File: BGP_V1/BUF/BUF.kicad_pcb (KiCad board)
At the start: 2 copper layers, 30 x 30 mm, 23 parts, among them P1 CONN_01X05, P2 CONN_01X02, P3 CONN_01X12, U1 MC33178, U2 TLV170

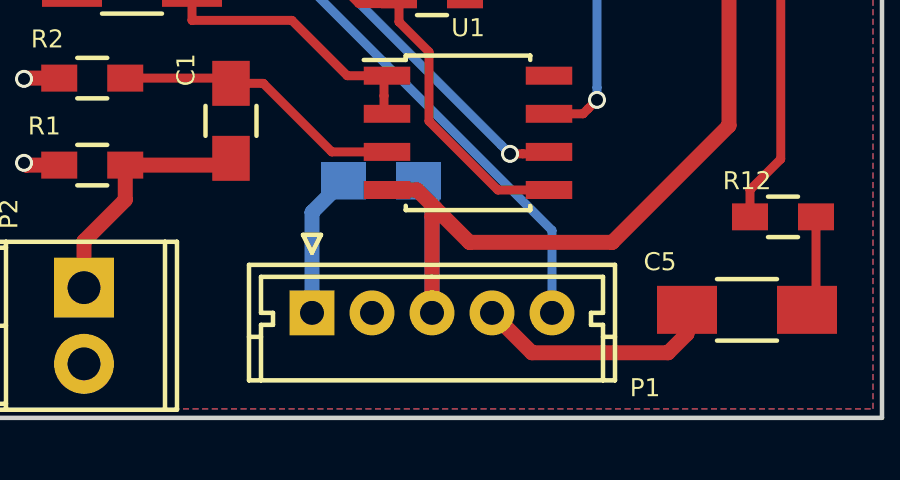
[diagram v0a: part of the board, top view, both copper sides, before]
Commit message: Gerbers
Mainly getting gerbers ready.  Issue with pots overlapping other boards in silk screens - top and bottom.
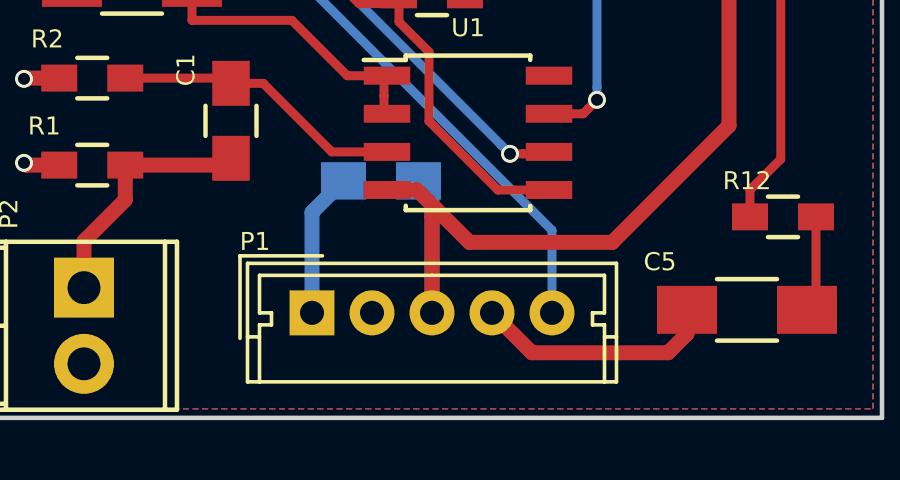
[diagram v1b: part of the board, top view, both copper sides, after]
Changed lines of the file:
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@@
-(kicad_pcb (version 4) (host pcbnew 4.0.4-1.fc24-product)
+(kicad_pcb (version 4) (host pcbnew 4.0.7)
   (general
     (links 49)
     (no_connects 0)
-    (area 135.10412 74.424999 167.075001 122.285001)
+    (area 135.10412 74.424999 167.075001 122.779999)
     (thickness 1.6)
     (drawings 9)
@@
       (drillshape 0)
       (scaleselection 1)
-      (outputdirectory ../../BGP/GERBER/BUF_1/))
+      (outputdirectory ../../GERBER/BUF_1/))
   )
   (net 0 "")
@@
     )
   )
-  (module Connectors_Molex:Molex_MicroLatch-53253-0570_05x2.00mm_Straight (layer F.Cu)
-    (at 148 118.5)
-    (descr "Molex Micro-Latch connector, PN:53253-0570, top entry type, through hole")
-    (tags "conn molex micro latch")
-    (fp_text reference P1 (at 11.1 2.5) (layer F.SilkS)
-      (effects (font (size 0.6 0.6) (thickness 0.15)))
-    )
-    (fp_text value CONN_01X05 (at 4 -3.5) (layer F.Fab) hide
-      (effects (font (size 0.6 0.6) (thickness 0.15)))
-    )
-    (fp_line (start -2.6 -2.1) (end -2.6 2.75) (layer F.CrtYd) (width 0.05))
-    (fp_line (start -2.6 2.75) (end 10.55 2.75) (layer F.CrtYd) (width 0.05))
-    (fp_line (start 10.55 2.75) (end 10.55 -2.1) (layer F.CrtYd) (width 0.05))
-    (fp_line (start 10.55 -2.1) (end -2.6 -2.1) (layer F.CrtYd) (width 0.05))
-    (fp_line (start -2.1 -1.6) (end -2.1 2.25) (layer F.SilkS) (width 0.15))
-    (fp_line (start -2.1 2.25) (end 10.1 2.25) (layer F.SilkS) (width 0.15))
-    (fp_line (start 10.1 2.25) (end 10.1 -1.6) (layer F.SilkS) (width 0.15))
-    (fp_line (start 10.1 -1.6) (end -2.1 -1.6) (layer F.SilkS) (width 0.15))
-    (fp_line (start 0 -2) (end -0.3 -2.6) (layer F.SilkS) (width 0.15))
-    (fp_line (start -0.3 -2.6) (end 0.3 -2.6) (layer F.SilkS) (width 0.15))
-    (fp_line (start 0.3 -2.6) (end 0 -2) (layer F.SilkS) (width 0.15))
-    (fp_line (start -2.1 0.8) (end -1.7 0.8) (layer F.SilkS) (width 0.15))
-    (fp_line (start 10.1 0.8) (end 9.7 0.8) (layer F.SilkS) (width 0.15))
-    (fp_line (start 4 -1.2) (end -1.7 -1.2) (layer F.SilkS) (width 0.15))
-    (fp_line (start -1.7 -1.2) (end -1.7 0) (layer F.SilkS) (width 0.15))
-    (fp_line (start -1.7 0) (end -1.3 0) (layer F.SilkS) (width 0.15))
-    (fp_line (start -1.3 0) (end -1.3 0.4) (layer F.SilkS) (width 0.15))
-    (fp_line (start -1.3 0.4) (end -1.7 0.4) (layer F.SilkS) (width 0.15))
-    (fp_line (start -1.7 0.4) (end -1.7 2.25) (layer F.SilkS) (width 0.15))
-    (fp_line (start 4 -1.2) (end 9.7 -1.2) (layer F.SilkS) (width 0.15))
-    (fp_line (start 9.7 -1.2) (end 9.7 0) (layer F.SilkS) (width 0.15))
-    (fp_line (start 9.7 0) (end 9.3 0) (layer F.SilkS) (width 0.15))
-    (fp_line (start 9.3 0) (end 9.3 0.4) (layer F.SilkS) (width 0.15))
-    (fp_line (start 9.3 0.4) (end 9.7 0.4) (layer F.SilkS) (width 0.15))
-    (fp_line (start 9.7 0.4) (end 9.7 2.25) (layer F.SilkS) (width 0.15))
-    (pad 1 thru_hole rect (at 0 0) (size 1.5 1.5) (drill 0.8) (layers *.Cu *.Mask)
-      (net 11 /V+))
-    (pad 2 thru_hole circle (at 2 0) (size 1.5 1.5) (drill 0.8) (layers *.Cu *.Mask)
-      (net 8 Earth))
-    (pad 3 thru_hole circle (at 4 0) (size 1.5 1.5) (drill 0.8) (layers *.Cu *.Mask)
-      (net 12 /V-))
-    (pad 4 thru_hole circle (at 6 0) (size 1.5 1.5) (drill 0.8) (layers *.Cu *.Mask)
-      (net 9 /OUT))
-    (pad 5 thru_hole circle (at 8 0) (size 1.5 1.5) (drill 0.8) (layers *.Cu *.Mask)
-      (net 18 /BUF_O))
-    (model Connectors_Molex.3dshapes/Molex_MicroLatch-53253-0570_05x2.00mm_Straight.wrl
-      (at (xyz 0 0 0))
-      (scale (xyz 1 1 1))
-      (rotate (xyz 0 0 0))
-    )
-  )
   (module Terminal_Blocks:TerminalBlock_Pheonix_MPT-2.54mm_2pol (layer F.Cu)
     (at 140.4 117.66 270)
@@
       (at (xyz 0 0 0))
       (scale (xyz 1 1 1))
+      (rotate (xyz 0 0 0))
+    )
+  )
+  (module Connectors_Molex:Molex_MicroLatch-53253-0570_05x2.00mm_Straight (layer F.Cu)
+    (at 148 118.5)
+    (descr "Molex Micro-Latch connector, PN:53253-0570, top entry type, through hole")
+    (tags "conn molex micro latch")
+    (fp_text reference P1 (at -1.9 -2.375001) (layer F.SilkS)
+      (effects (font (size 0.6 0.6) (thickness 0.15)))
+    )
+    (fp_text value CONN_01X05 (at 3.7 3.424999) (layer F.Fab) hide
+      (effects (font (size 0.6 0.6) (thickness 0.15)))
+    )
+    (fp_line (start -2 -1.5) (end -2 2.15) (layer F.Fab) (width 0.1))
+    (fp_line (start -2 2.15) (end 10 2.15) (layer F.Fab) (width 0.1))
+    (fp_line (start 10 2.15) (end 10 -1.5) (layer F.Fab) (width 0.1))
+    (fp_line (start 10 -1.5) (end -2 -1.5) (layer F.Fab) (width 0.1))
+    (fp_line (start -2.6 -2.1) (end -2.6 2.75) (layer F.CrtYd) (width 0.05))
+    (fp_line (start -2.6 2.75) (end 10.65 2.75) (layer F.CrtYd) (width 0.05))
+    (fp_line (start 10.65 2.75) (end 10.65 -2.1) (layer F.CrtYd) (width 0.05))
+    (fp_line (start 10.65 -2.1) (end -2.6 -2.1) (layer F.CrtYd) (width 0.05))
+    (fp_line (start -2.15 -1.65) (end -2.15 2.3) (layer F.SilkS) (width 0.12))
+    (fp_line (start -2.15 2.3) (end 10.15 2.3) (layer F.SilkS) (width 0.12))
+    (fp_line (start 10.15 2.3) (end 10.15 -1.65) (layer F.SilkS) (width 0.12))
+    (fp_line (start 10.15 -1.65) (end -2.15 -1.65) (layer F.SilkS) (width 0.12))
+    (fp_line (start 0.35 -1.9) (end -2.4 -1.9) (layer F.SilkS) (width 0.12))
+    (fp_line (start -2.4 -1.9) (end -2.4 0.85) (layer F.SilkS) (width 0.12))
+    (fp_line (start 0.35 -1.9) (end -2.4 -1.9) (layer F.Fab) (width 0.1))
+    (fp_line (start -2.4 -1.9) (end -2.4 0.85) (layer F.Fab) (width 0.1))
+    (fp_line (start -2.15 0.8) (end -1.75 0.8) (layer F.SilkS) (width 0.12))
+    (fp_line (start 10.15 0.8) (end 9.75 0.8) (layer F.SilkS) (width 0.12))
+    (fp_line (start 4 -1.25) (end -1.75 -1.25) (layer F.SilkS) (width 0.12))
+    (fp_line (start -1.75 -1.25) (end -1.75 0) (layer F.SilkS) (width 0.12))
+    (fp_line (start -1.75 0) (end -1.35 0) (layer F.SilkS) (width 0.12))
+    (fp_line (start -1.35 0) (end -1.35 0.4) (layer F.SilkS) (width 0.12))
+    (fp_line (start -1.35 0.4) (end -1.75 0.4) (layer F.SilkS) (width 0.12))
+    (fp_line (start -1.75 0.4) (end -1.75 2.3) (layer F.SilkS) (width 0.12))
+    (fp_line (start 4 -1.25) (end 9.75 -1.25) (layer F.SilkS) (width 0.12))
+    (fp_line (start 9.75 -1.25) (end 9.75 0) (layer F.SilkS) (width 0.12))
+    (fp_line (start 9.75 0) (end 9.35 0) (layer F.SilkS) (width 0.12))
+    (fp_line (start 9.35 0) (end 9.35 0.4) (layer F.SilkS) (width 0.12))
+    (fp_line (start 9.35 0.4) (end 9.75 0.4) (layer F.SilkS) (width 0.12))
+    (fp_line (start 9.75 0.4) (end 9.75 2.3) (layer F.SilkS) (width 0.12))
+    (fp_text user %R (at 4 1.5) (layer F.Fab) hide
+      (effects (font (size 0.6 0.6) (thickness 0.15)))
+    )
+    (pad 1 thru_hole rect (at 0 0) (size 1.5 1.5) (drill 0.8) (layers *.Cu *.Mask)
+      (net 11 /V+))
+    (pad 2 thru_hole circle (at 2 0) (size 1.5 1.5) (drill 0.8) (layers *.Cu *.Mask)
+      (net 8 Earth))
+    (pad 3 thru_hole circle (at 4 0) (size 1.5 1.5) (drill 0.8) (layers *.Cu *.Mask)
+      (net 12 /V-))
+    (pad 4 thru_hole circle (at 6 0) (size 1.5 1.5) (drill 0.8) (layers *.Cu *.Mask)
+      (net 9 /OUT))
+    (pad 5 thru_hole circle (at 8 0) (size 1.5 1.5) (drill 0.8) (layers *.Cu *.Mask)
+      (net 18 /BUF_O))
+    (model ${KISYS3DMOD}/Connectors_Molex.3dshapes/Molex_MicroLatch-53253-0570_05x2.00mm_Straight.wrl
+      (at (xyz 0 0 0))
+      (scale (xyz 1 1 1))

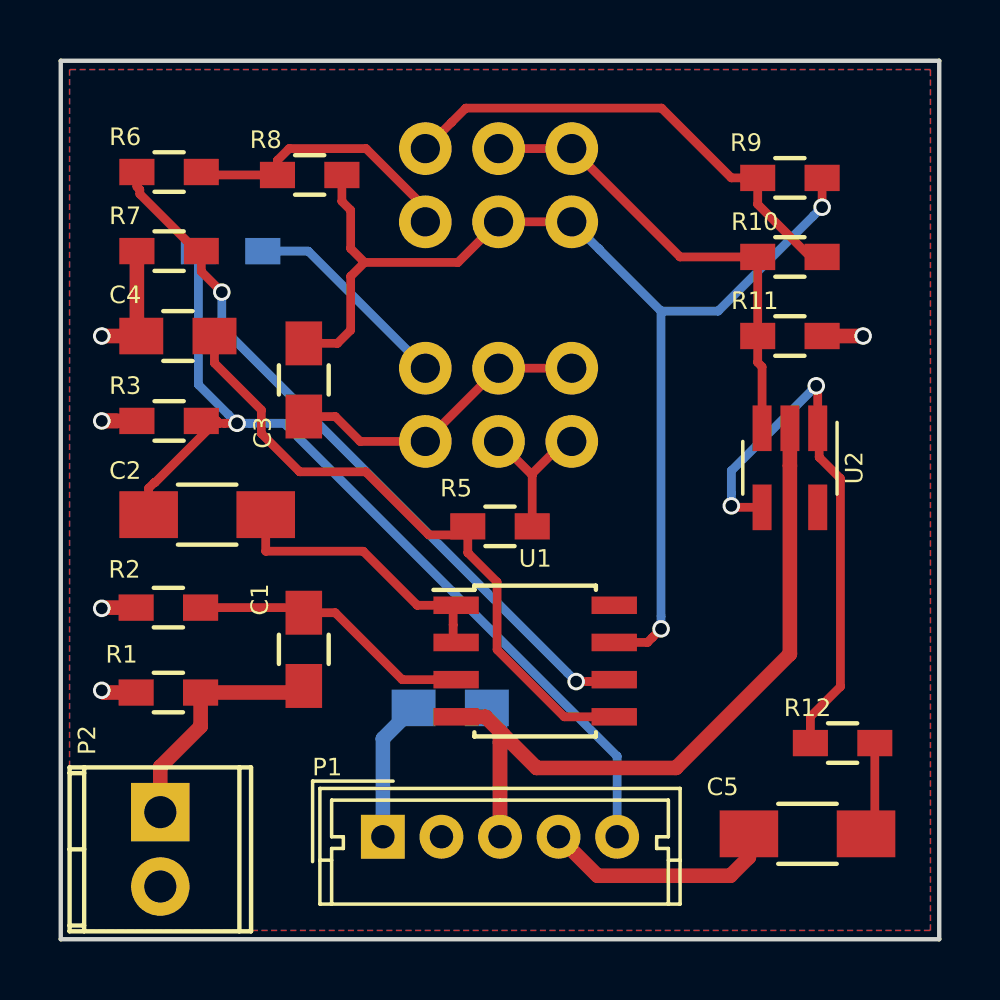
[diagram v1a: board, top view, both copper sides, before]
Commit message: Pot fixups for silkscreen overlap
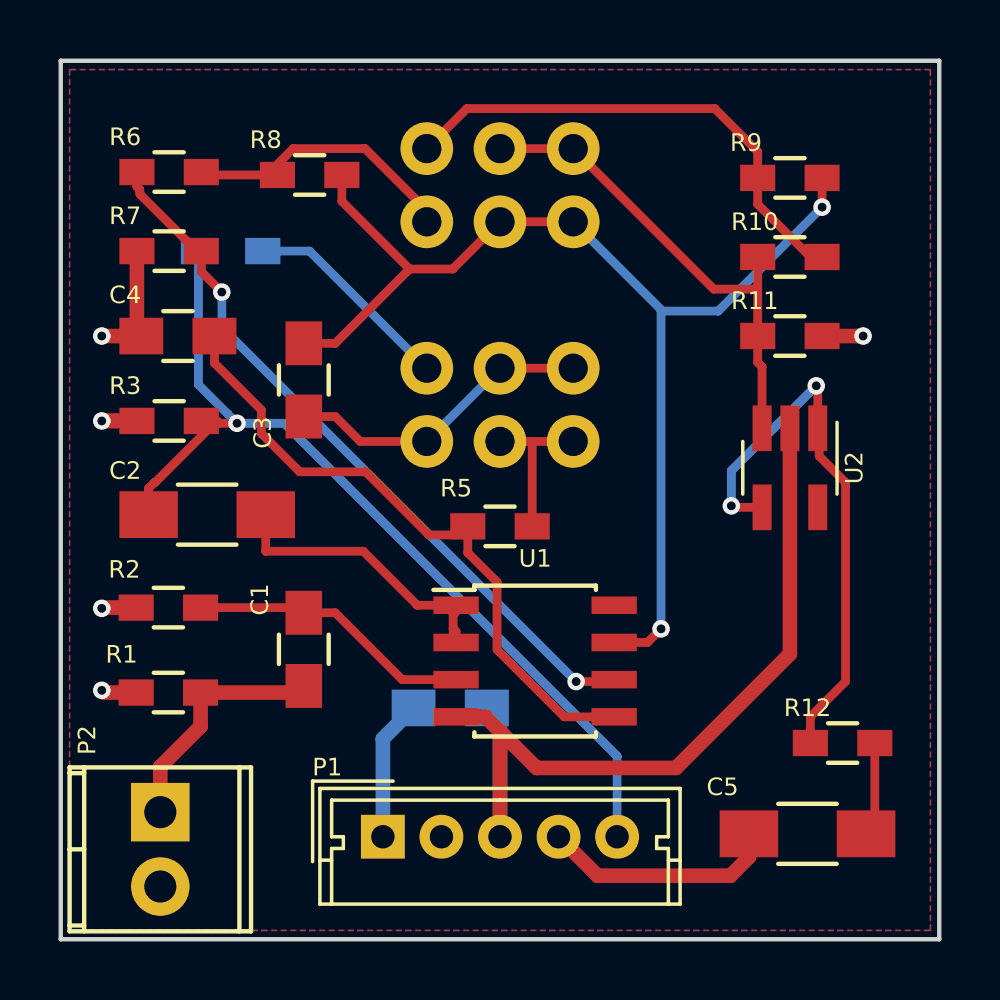
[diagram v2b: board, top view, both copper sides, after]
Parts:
- moved P3 5.50 mm to (149.5, 95.0)
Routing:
- net Net-(C2-Pad1): track 9.68 -> 10.6 mm
- net /VP2_2: track 40.9 -> 40.1 mm

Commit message: Concentric pot fixups for 1_BUF
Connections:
- P3 pad 1: /VP1_1 -> /VF1_1
- P3 pad 10: /VF1_2 -> /VP2_1
- P3 pad 11: /VF2_2 -> /VP2_1
- P3 pad 12: /VF2_2 -> /VP2_2
- P3 pad 2: /VP1_2 -> /VF1_1
- P3 pad 3: /VP1_2 -> /VF1_2
- P3 pad 4: /VP2_1 -> /VF1_2
- P3 pad 5: /VP2_2 -> /VF1_2
- P3 pad 6: /VP2_2 -> /VF2_2
- P3 pad 7: /VF1_1 -> /VP1_1
- P3 pad 8: /VF1_2 -> /VP1_1
- P3 pad 9: /VF1_2 -> /VP1_2
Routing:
- net /VF2_2: track 5.40 -> 12.8 mm, vias 0 -> 1
- net /VP2_2: track 40.1 -> 47.3 mm, vias 2 -> 0
- net /VP2_1: track 9.74 -> 16.7 mm, vias 0 -> 1
- net /VF1_2: track 10.6 -> 15.6 mm, vias 0 -> 1
- net /VP1_2: track 16.7 -> 12.3 mm
- net /V-: track 29.7 -> 32.6 mm, vias 0 -> 1
- net /VF1_1: track 7.26 -> 10.1 mm
